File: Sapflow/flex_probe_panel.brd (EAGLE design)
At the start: 57 x 11 mm, 5 parts

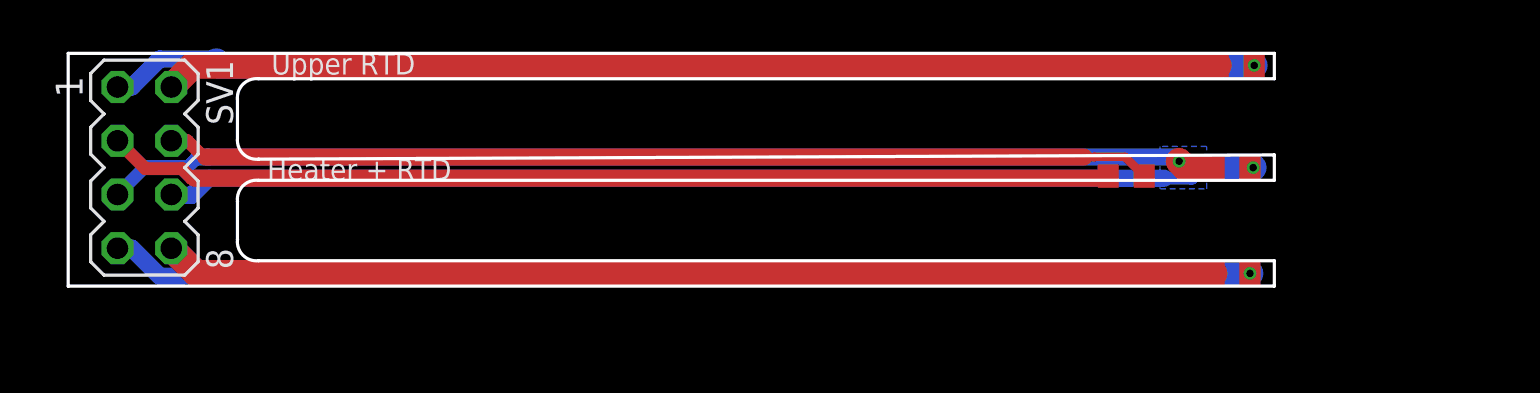
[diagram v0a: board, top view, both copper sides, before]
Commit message: Made flex probe thinner
Also made a panel layout, so we can fit more PCBs into the same area.
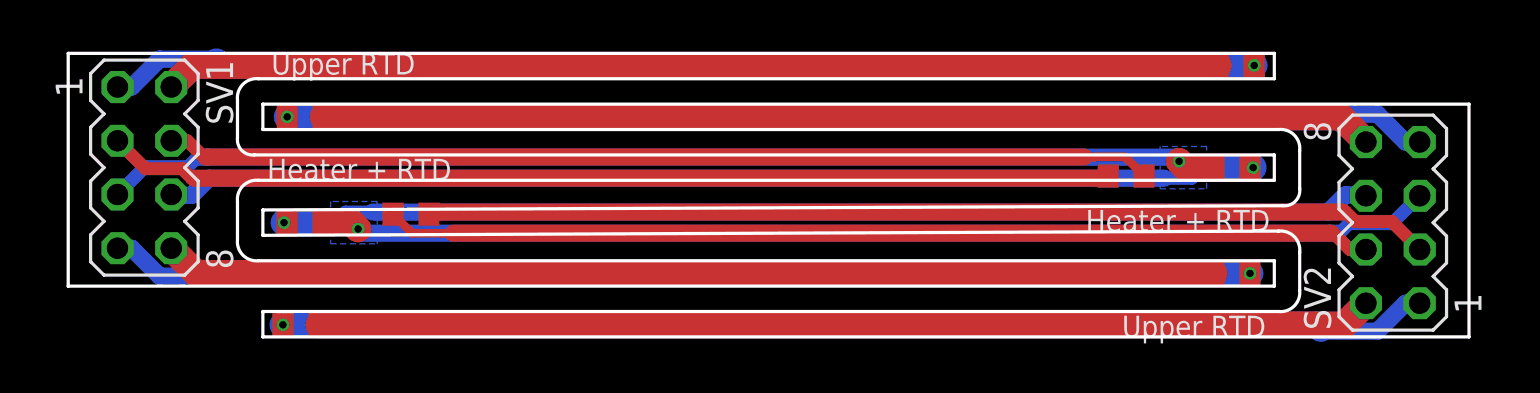
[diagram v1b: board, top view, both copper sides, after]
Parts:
- added R5, R6, R8: RTD, resistor:R0603
- added R7: 100, resistor:R0603
- added SV2: (no value), con-lstb:MA04-2
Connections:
- new net N$10: R8.1, SV2.7
- new net N$12: R7.2, SV2.6
- new net N$13: R7.1, SV2.5
- new net N$14: R5.2, SV2.2
- new net N$15: R5.1, SV2.1
- new net N$16: R8.2, SV2.8
- new net N$5: R6.2, SV2.4
- new net N$6: R6.1, SV2.3
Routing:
- net N$15: track 0.00 -> 54.4 mm, vias 0 -> 1
- net N$10: track 0.00 -> 54.1 mm, vias 0 -> 1
- net N$13: track 0.00 -> 53.3 mm, vias 0 -> 1
- net N$12: track 0.00 -> 51.8 mm, vias 0 -> 1
- net N$14: track 0.00 -> 49.9 mm
- net N$16: track 0.00 -> 49.8 mm
- net N$6: track 0.00 -> 47.6 mm
- net N$5: track 0.00 -> 46.7 mm
- added copper zone on layer 16, net N$12
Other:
- board size 57 x 11 mm -> 66.2 x 13.4 mm
- board text removed: "1"
- board text removed: "2"
- board text removed: "3"
- board text removed: "4"
